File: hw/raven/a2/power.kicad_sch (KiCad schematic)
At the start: 28 parts, among them J1 ATX Power, J202 Pinhdr_02x05, J203 Pinhdr_01x03, J305 FanHeader, SW201 SW_Push, SW202 SW_Push, U201 LM7905CT_NOPB, U202 MAX16054AZT+T, U203 DS1818, U204 74HCT10

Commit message: Raven.A2 : routing cleanup + gpio
pwr switch status -> uart gpi
uart gpo -> header
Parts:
- J202: footprint Connector_PinHeader_2.54mm:PinHeader_2x05_P2.54mm_Vertical -> Connector_PinHeader_2.54mm:PinHeader_2x04_P2.54mm_Vertical; symbol Connector_Generic:Conn_02x05_Odd_Even -> Connector_Generic:Conn_02x04_Odd_Even
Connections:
- net PWRSW+ renamed PWR_SW
- no-connect marks 7 -> 5
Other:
- moved on the sheet: C201, SW201, U202

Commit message: Raven.A2: pullups on MC68150 databus
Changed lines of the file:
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@@
     (effects (font (size 1.27 1.27)) (justify left top))
-  )
-  (text_box "TODO:\nPWRSW+ to spare GPI on uart\nTo read power button state"
-    (at -3.175 29.845 0) (size 34.925 11.43)
-    (stroke (width 0) (type default))
-    (fill (type color) (color 255 230 63 0.53))
-    (effects (font (size 1.27 1.27) (color 0 0 0 1)) (justify left top))
   )
   (text_box "Fan connector (5V)"

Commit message: rev.A2 updates
Added i2c DAC for reading cpu core temperature
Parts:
- added R201: 10K, Resistor_SMD:R_1206_3216Metric_Pad1.30x1.75mm_HandSolder, symbol Device:R
- renumbered R201 to R202, R202 to R203, R204 to R205, R205 to R206, R206 to R207, R207 to R208, R208 to R209
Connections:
- net +5VL: now also R201.2
- net PWR_SW: now also R201.1

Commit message: Raven.A2 wip
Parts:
- removed R205: 10K, Resistor_SMD:R_1206_3216Metric_Pad1.30x1.75mm_HandSolder, symbol Device:R
- J202: value Pinhdr_02x05 -> Pinhdr_02x04; Manufacturer_Part_Number 61301021121 -> 61300821121
- renumbered C1 to C205, D1 to D201, D2 to D202, D3 to D203, J1 to J201, J305 to J204, J305 to J205, J305 to J206, R3 to R204

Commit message: replaced DS1818 TH part with SMD version
It's easy to get the orientation wrong on the TH part, there is no question about it when using the SMD part.
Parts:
- U203: footprint 68k:DS1813 -> Package_TO_SOT_SMD:SOT-23-3; Manufacturer_Part_Number DS1818-10+T&R -> DS1818R-10+T&R; Mouser Part Number 700-DS1818-10T&R -> 700-DS1818R-10T&R
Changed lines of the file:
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@@
 			)
 		)
-		(property "Footprint" "68k:DS1813"
+		(property "Footprint" "Package_TO_SOT_SMD:SOT-23-3"
 			(at 55.88 200.965 0)
 			(effects
@@
 			)
 		)
-		(property "Mouser Part Number" "700-DS1818-10T&R"
+		(property "Mouser Part Number" "700-DS1818R-10T&R"
 			(at 55.88 600.965 0)
 			(effects
@@
 			)
 		)
-		(property "Manufacturer_Part_Number" "DS1818-10+T&R"
+		(property "Manufacturer_Part_Number" "DS1818R-10+T&R"
 			(at 55.88 900.965 0)
 			(effects

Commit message: a2 wip
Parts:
- renumbered R206 to R205, R207 to R206, R208 to R207, R209 to R208
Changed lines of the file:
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@@
 		)
 	)
-	(text_box "TODO:\nSMD leds on motherboard?"
-		(exclude_from_sim no)
-		(at 147.32 27.305 0)
-		(size 31.115 11.43)
-		(margins 0.9525 0.9525 0.9525 0.9525)
-		(stroke
-			(width 0)
-			(type default)
-		)
-		(fill
-			(type color)
-			(color 255 230 63 0.53)
-		)
-		(effects
-			(font
-				(size 1.27 1.27)
-				(color 0 0 0 1)
-			)
-			(justify left top)
-		)
-	)
 	(text_box "Reset circuit and switch"
 		(exclude_from_sim no)
@@
 		(on_board yes)
 		(dnp no)
-		(property "Reference" "R206"
+		(property "Reference" "R205"
 			(at 184.15 103.505 90)
 			(effects
@@
 			(project "raven"
 				(path "/af55e73e-5814-45b4-ac5c-0bab62c0b1c7/3edf683f-0a35-4a7c-880a-e714e6e1adf2"
-					(reference "R206")
+					(reference "R205")
 					(unit 1)
 				)
@@
 		(dnp no)
 		(fields_autoplaced yes)
-		(property "Reference" "#PWR0238"
+		(property "Reference" "#PWR0237"
 			(at 114.935 178.435 0)
 			(effects
@@
 			(project "raven"
 				(path "/af55e73e-5814-45b4-ac5c-0bab62c0b1c7/3edf683f-0a35-4a7c-880a-e714e6e1adf2"
-					(reference "#PWR0238")
+					(reference "#PWR0237")
 					(unit 1)
 				)
@@
 		(on_board yes)
 		(dnp no)
-		(property "Reference" "#PWR0228"
+		(property "Reference" "#PWR0227"
 			(at 150.495 114.3 0)
 			(effects
@@
 			(project "raven"
 				(path "/af55e73e-5814-45b4-ac5c-0bab62c0b1c7/3edf683f-0a35-4a7c-880a-e714e6e1adf2"
-					(reference "#PWR0228")
+					(reference "#PWR0227")
 					(unit 1)
 				)
@@
 		(on_board yes)
 		(dnp no)
-		(property "Reference" "R208"
+		(property "Reference" "R207"
 			(at 147.955 113.03 90)
 			(effects
@@
 			(project "raven"
 				(path "/af55e73e-5814-45b4-ac5c-0bab62c0b1c7/3edf683f-0a35-4a7c-880a-e714e6e1adf2"
-					(reference "R208")
+					(reference "R207")
 					(unit 1)
 				)
@@
 		(on_board yes)
 		(dnp no)
-		(property "Reference" "#PWR0226"
+		(property "Reference" "#PWR0225"
 			(at 184.15 106.045 0)
 			(effects
@@
 			(project "raven"
 				(path "/af55e73e-5814-45b4-ac5c-0bab62c0b1c7/3edf683f-0a35-4a7c-880a-e714e6e1adf2"
-					(reference "#PWR0226")
+					(reference "#PWR0225")
 					(unit 1)
 				)
@@
 		(on_board yes)
 		(dnp no)
-		(property "Reference" "R207"
+		(property "Reference" "R206"
 			(at 145.415 113.03 90)
 			(effects
@@
 			(project "raven"
 				(path "/af55e73e-5814-45b4-ac5c-0bab62c0b1c7/3edf683f-0a35-4a7c-880a-e714e6e1adf2"
-					(reference "R207")
+					(reference "R206")
 					(unit 1)
 				)
@@
 		(on_board yes)
 		(dnp no)
-		(property "Reference" "#PWR0229"
+		(property "Reference" "#PWR0228"
 			(at 249.555 125.095 0)
 			(effects
@@
 			(project "raven"
 				(path "/af55e73e-5814-45b4-ac5c-0bab62c0b1c7/3edf683f-0a35-4a7c-880a-e714e6e1adf2"
-					(reference "#PWR0229")
+					(reference "#PWR0228")
 					(unit 1)
 				)
@@
 		(on_board yes)
 		(dnp no)
-		(property "Reference" "#PWR0227"
+		(property "Reference" "#PWR0226"
 			(at 249.555 98.425 0)
 			(effects
@@
 			(project "raven"
 				(path "/af55e73e-5814-45b4-ac5c-0bab62c0b1c7/3edf683f-0a35-4a7c-880a-e714e6e1adf2"
-					(reference "#PWR0227")
+					(reference "#PWR0226")
 					(unit 1)
 				)
@@
 		(dnp no)
 		(fields_autoplaced yes)
-		(property "Reference" "#PWR0236"
+		(property "Reference" "#PWR0235"
 			(at 34.29 178.435 0)
 			(effects
@@
 			(project "raven"
 				(path "/af55e73e-5814-45b4-ac5c-0bab62c0b1c7/3edf683f-0a35-4a7c-880a-e714e6e1adf2"
-					(reference "#PWR0236")
+					(reference "#PWR0235")
 					(unit 1)
 				)
@@
 		(on_board yes)
 		(dnp no)
-		(property "Reference" "#PWR0235"
+		(property "Reference" "#PWR0234"
 			(at 114.935 164.465 0)
 			(effects
@@
 			(project "raven"
 				(path "/af55e73e-5814-45b4-ac5c-0bab62c0b1c7/3edf683f-0a35-4a7c-880a-e714e6e1adf2"
-					(reference "#PWR0235")
+					(reference "#PWR0234")
 					(unit 1)
 				)
@@
 		(on_board yes)
 		(dnp no)
-		(property "Reference" "R209"
+		(property "Reference" "R208"
 			(at 150.495 113.03 90)
 			(effects
@@
 			(project "raven"
 				(path "/af55e73e-5814-45b4-ac5c-0bab62c0b1c7/3edf683f-0a35-4a7c-880a-e714e6e1adf2"
-					(reference "R209")
+					(reference "R208")
 					(unit 1)
 				)
@@
 		(on_board yes)
 		(dnp no)
-		(property "Reference" "#PWR0233"
+		(property "Reference" "#PWR0232"
 			(at 34.29 164.465 0)
 			(effects
@@
 			(project "raven"
 				(path "/af55e73e-5814-45b4-ac5c-0bab62c0b1c7/3edf683f-0a35-4a7c-880a-e714e6e1adf2"
-					(reference "#PWR0233")
+					(reference "#PWR0232")
 					(unit 1)
 				)
@@
 		(dnp no)
 		(fields_autoplaced yes)
-		(property "Reference" "#PWR0237"
+		(property "Reference" "#PWR0236"
 			(at 75.565 178.435 0)
 			(effects
@@
 			(project "raven"
 				(path "/af55e73e-5814-45b4-ac5c-0bab62c0b1c7/3edf683f-0a35-4a7c-880a-e714e6e1adf2"
-					(reference "#PWR0237")
+					(reference "#PWR0236")
 					(unit 1)
 				)
@@
 		(dnp no)
 		(fields_autoplaced yes)
-		(property "Reference" "#PWR0230"
+		(property "Reference" "#PWR0229"
 			(at 116.205 130.175 0)
 			(effects
@@
 			(project "raven"
 				(path "/af55e73e-5814-45b4-ac5c-0bab62c0b1c7/3edf683f-0a35-4a7c-880a-e714e6e1adf2"
-					(reference "#PWR0230")
+					(reference "#PWR0229")
 					(unit 1)
 				)
@@
 		(dnp no)
 		(fields_autoplaced yes)
-		(property "Reference" "#PWR0231"
+		(property "Reference" "#PWR0230"
 			(at 48.26 140.335 0)
 			(effects
@@
 			(project "raven"
 				(path "/af55e73e-5814-45b4-ac5c-0bab62c0b1c7/3edf683f-0a35-4a7c-880a-e714e6e1adf2"
-					(reference "#PWR0231")
+					(reference "#PWR0230")
 					(unit 1)
 				)
@@
 		(on_board yes)
 		(dnp no)
-		(property "Reference" "#PWR0234"
+		(property "Reference" "#PWR0233"
 			(at 75.565 164.465 0)
 			(effects
@@
 			(project "raven"
 				(path "/af55e73e-5814-45b4-ac5c-0bab62c0b1c7/3edf683f-0a35-4a7c-880a-e714e6e1adf2"
-					(reference "#PWR0234")
+					(reference "#PWR0233")
 					(unit 1)
 				)
@@
 		(dnp no)
 		(fields_autoplaced yes)
-		(property "Reference" "#PWR0232"
+		(property "Reference" "#PWR0231"
 			(at 80.645 140.335 0)
 			(effects
@@
 			(project "raven"
 				(path "/af55e73e-5814-45b4-ac5c-0bab62c0b1c7/3edf683f-0a35-4a7c-880a-e714e6e1adf2"
-					(reference "#PWR0232")
+					(reference "#PWR0231")
 					(unit 1)
 				)

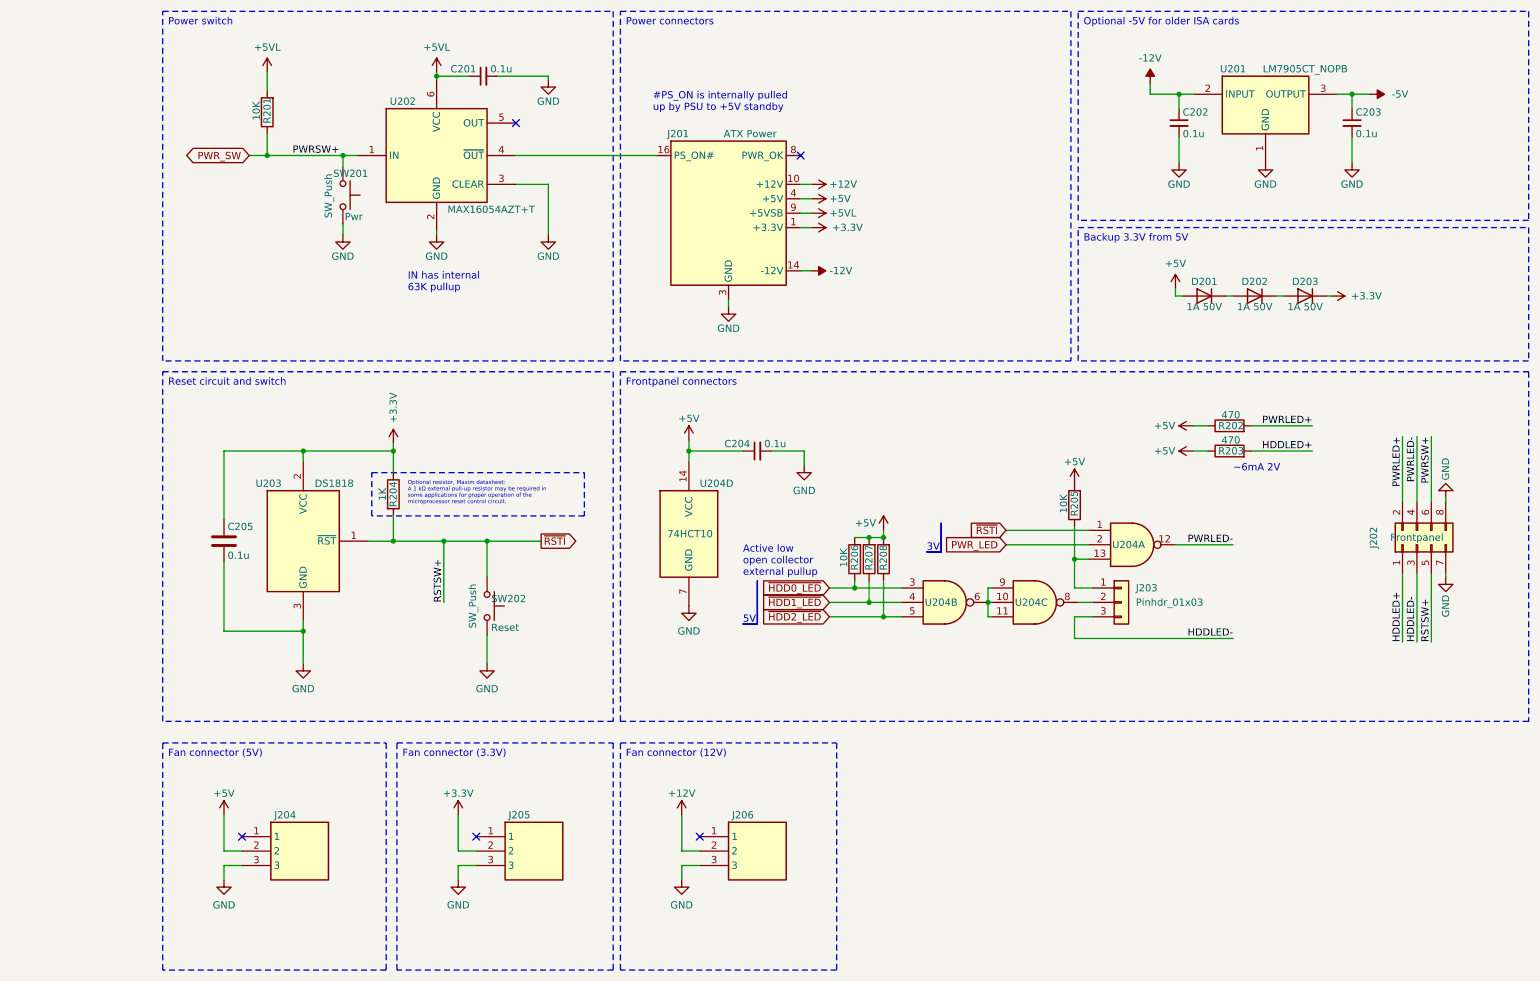
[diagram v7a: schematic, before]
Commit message: A2: DSP ram routing
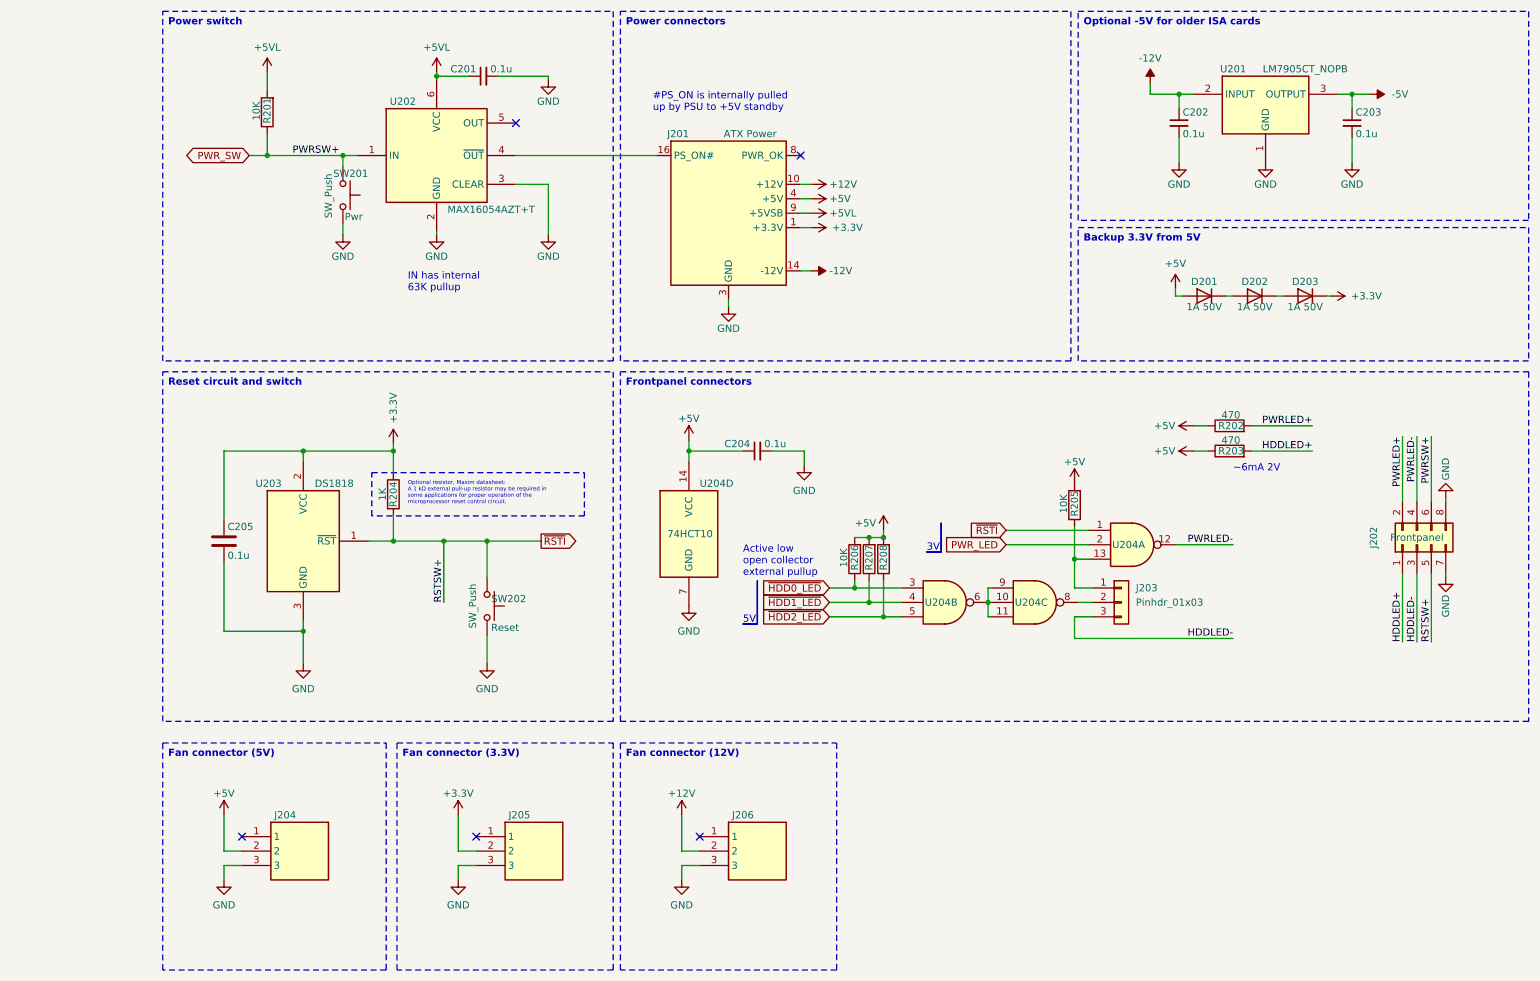
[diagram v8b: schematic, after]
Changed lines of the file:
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@@
 			(font
 				(size 1.27 1.27)
+				(thickness 0.254)
+				(bold yes)
 			)
 			(justify left top)
@@
 			(font
 				(size 1.27 1.27)
+				(thickness 0.254)
+				(bold yes)
 			)
 			(justify left top)
@@
 			(font
 				(size 1.27 1.27)
+				(thickness 0.254)
+				(bold yes)
 			)
 			(justify left top)
@@
 			(font
 				(size 1.27 1.27)
+				(thickness 0.254)
+				(bold yes)
 			)
 			(justify left top)
@@
 			(font
 				(size 1.27 1.27)
+				(thickness 0.254)
+				(bold yes)
 			)
 			(justify left top)
@@
 			(font
 				(size 1.27 1.27)
+				(thickness 0.254)
+				(bold yes)
 			)
 			(justify left top)
@@
 			(font
 				(size 1.27 1.27)
+				(thickness 0.254)
+				(bold yes)
 			)
 			(justify left top)
@@
 			(font
 				(size 1.27 1.27)
+				(thickness 0.254)
+				(bold yes)
 			)
 			(justify left top)
@@
 			(font
 				(size 1.27 1.27)
+				(thickness 0.254)
+				(bold yes)
 			)
 			(justify left top)
